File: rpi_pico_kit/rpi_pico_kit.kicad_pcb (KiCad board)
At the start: 2 copper layers, 99.1 x 99.1 mm, 195 parts, among them J1 DC Jack 5.5x2.1mm, J10 OLED Display SSD1306, J11 Conn_01x04_Male, J12 Conn_01x04_Male, J13 AudioJack-CUI-SJ-3523-SMT, J14 AudioJack-CUI-SJ-3523-SMT, J2 USB_B, J3 Conn_01x03_Male, J4 DB15_Female, J5 HDMI_A, J6 Conn_01x08_Male, J7 Conn_01x08_Male, J8 Conn_01x08_Male, J9 Micro_SD_Card_Det, Q1 DMN63D8L-7, Q2 DMN63D8L-7, Q3 DMN63D8L-7, Q4 DMN63D8L-7, Q5 DMN63D8L-7, Q6 DMN63D8L-7, Q7 DMN63D8L-7, SW1 SW_Push, SW10 SW_Push, SW2 RotaryEncoder_Switch, SW3 SW_Push, SW4 SW_Push, SW5 SW_Push, SW6 SW_Push, SW7 SW_Push, SW8 SW_Push, SW9 SW_Push, U1 RPi Pico, U10 74LVC2G34GV, U11 PCM5101A, U2 NCP1117-3.3_SOT223, U3 RP2040, U4 W25Q16JVSSIQ, U5 74HC14, U6 74HC14, U7 MCP23S08-xSO, U8 AT24CS32, U9 NCP115-3.3_SOT23-5, Y1 12MHz

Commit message: changed RPi Pico footprint in pcb
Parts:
- U1: footprint RPi_Pico:RPi_Pico_THT -> RPi_Pico:RPi_Pico_THT_socket

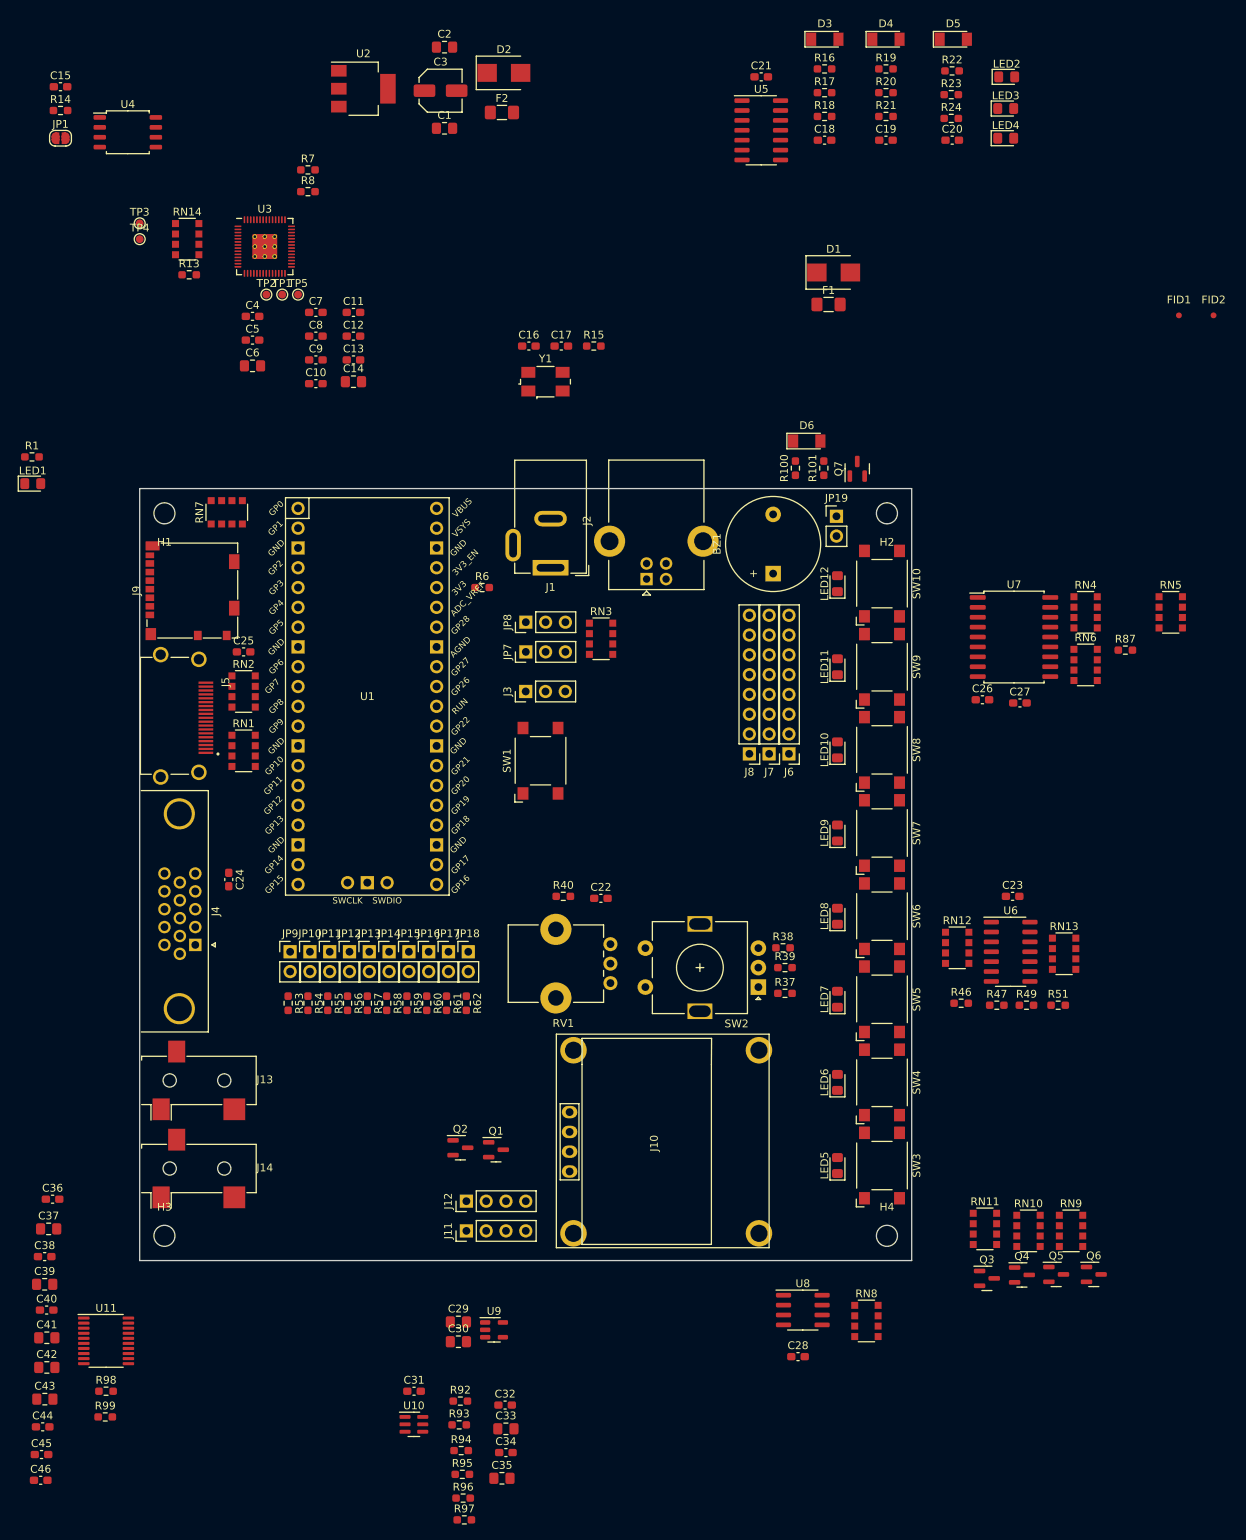
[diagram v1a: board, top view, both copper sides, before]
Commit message: changed footprints for resistor arrays
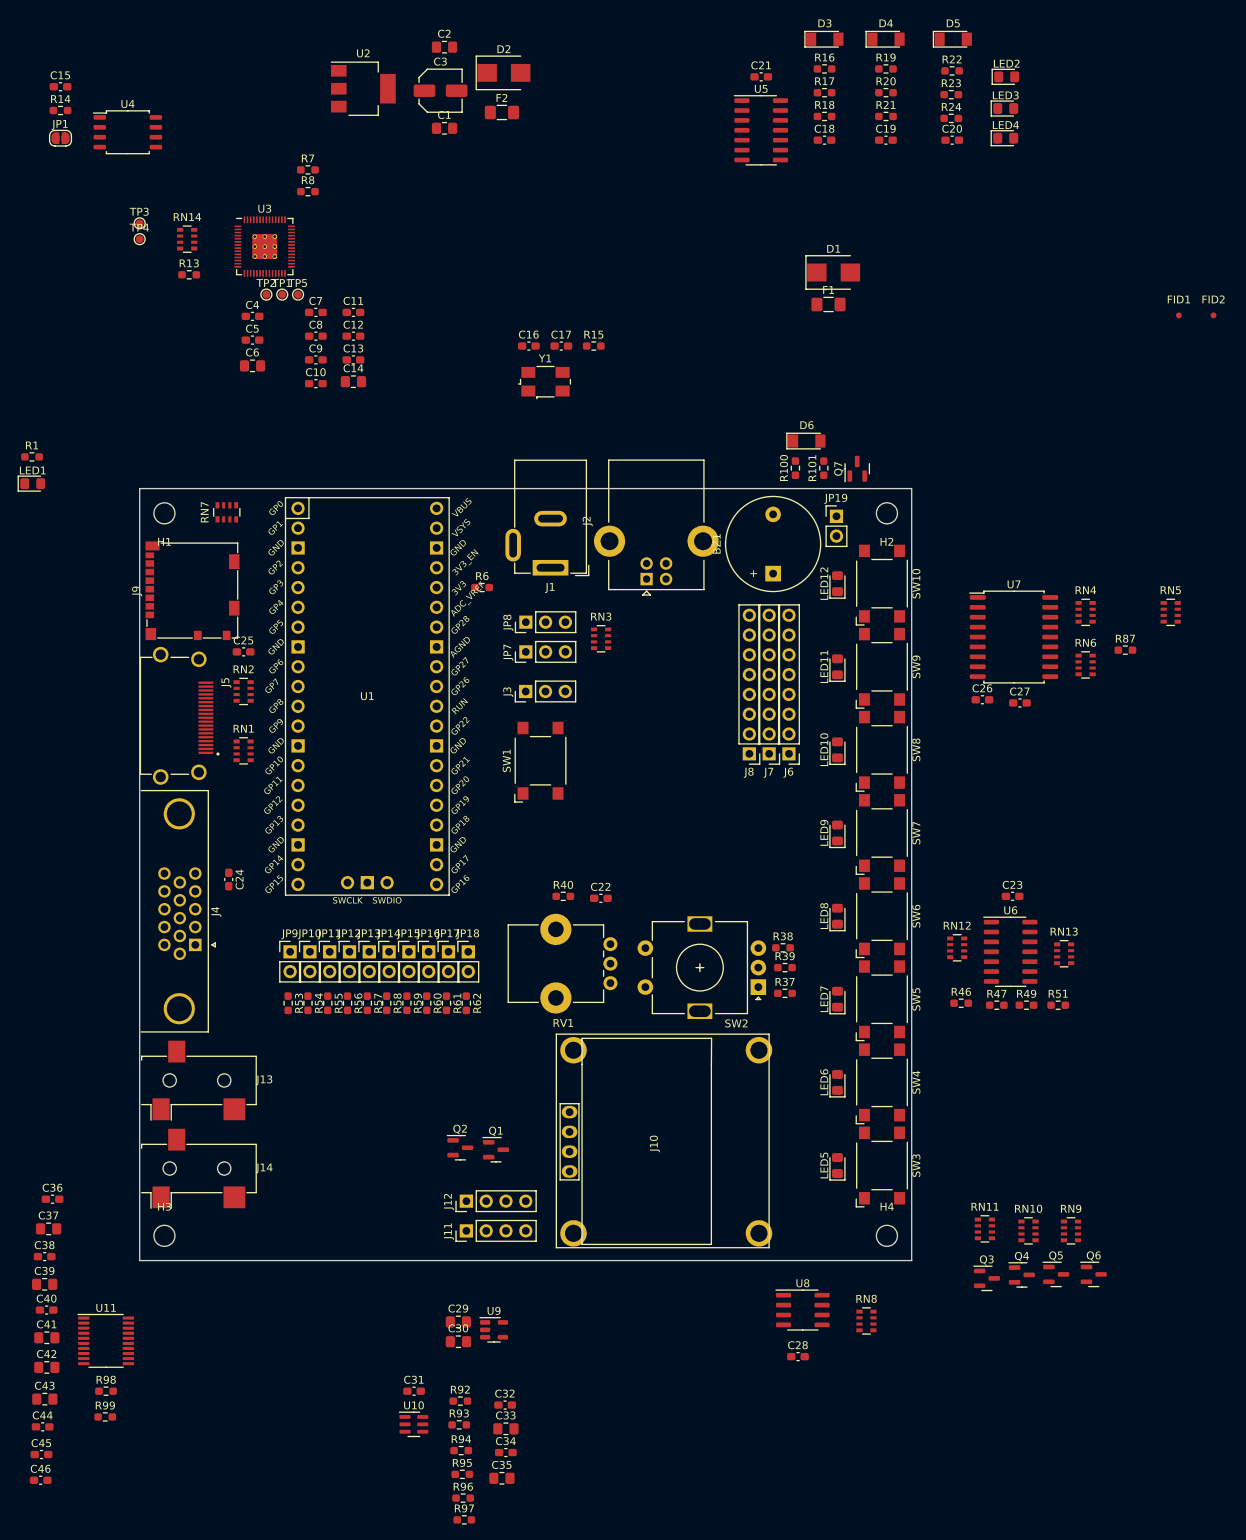
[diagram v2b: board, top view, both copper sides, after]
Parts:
- RN1, RN10, RN11, RN12, RN13, RN14, RN2, RN3, RN4, RN5, RN6, RN7, RN8, RN9: footprint Resistor_SMD:R_Array_Convex_4x1206 -> Resistor_SMD:R_Array_Convex_4x0603

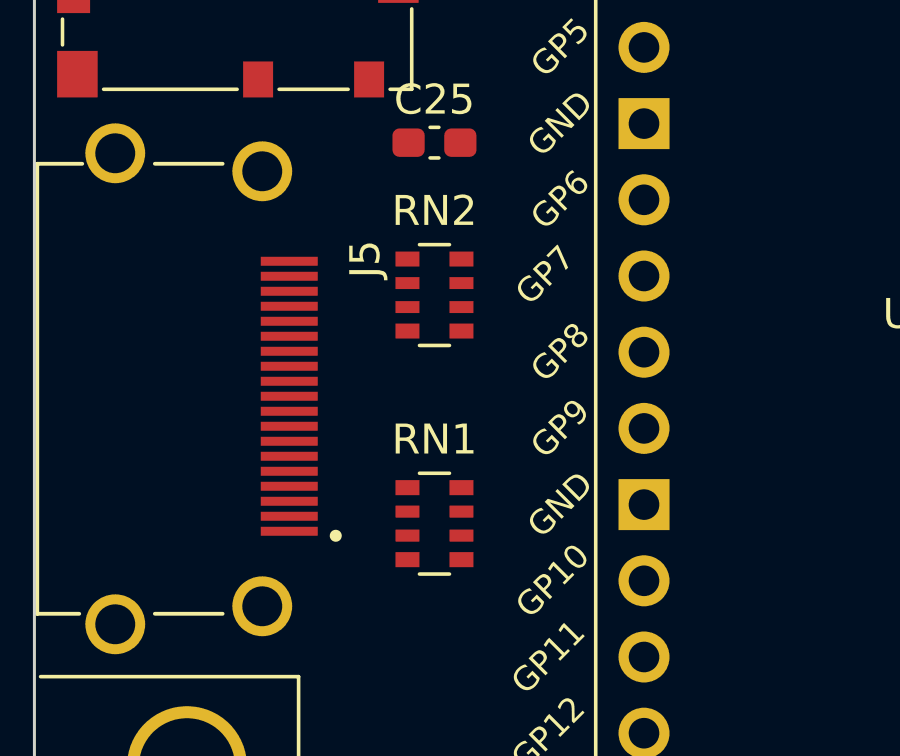
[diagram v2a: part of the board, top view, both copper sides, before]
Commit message: added names to differential pairs
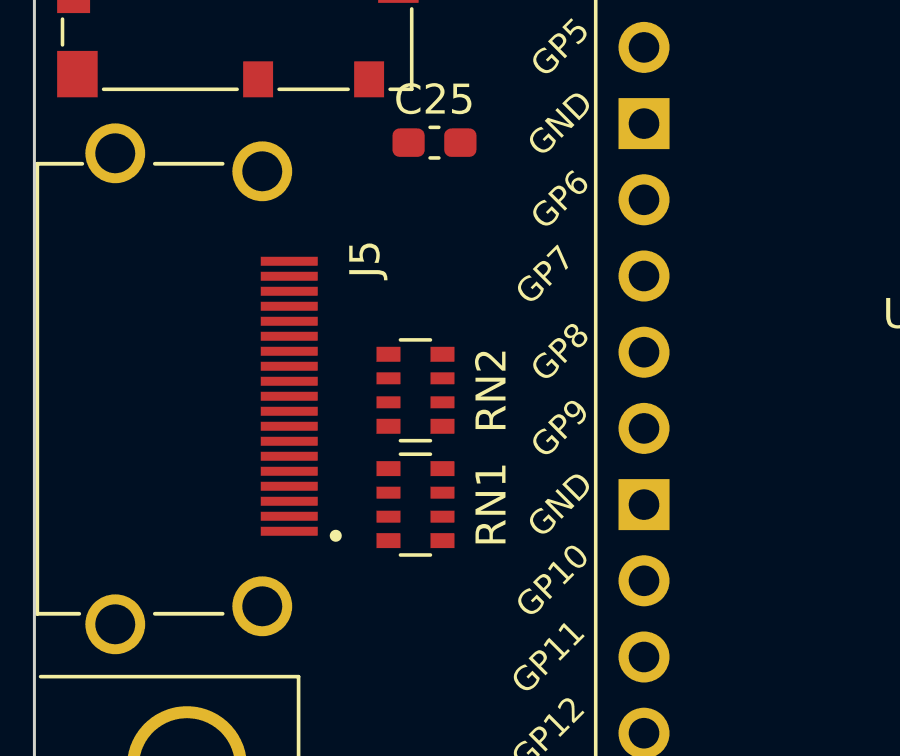
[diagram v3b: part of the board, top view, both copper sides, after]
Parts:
- moved RN2 3.24 mm to (50.8, 67.3)
- moved RN1 0.90 mm to (50.8, 71.1)
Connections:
- net Net-(J5-CK+) renamed /VGA & DVI Interface/_CLK+
- net Net-(J5-CK-) renamed /VGA & DVI Interface/_CLK-
- net Net-(J5-D0+) renamed /VGA & DVI Interface/_D0+
- net Net-(J5-D0-) renamed /VGA & DVI Interface/_D0-
- net Net-(J5-D1+) renamed /VGA & DVI Interface/_D1+
- net Net-(J5-D1-) renamed /VGA & DVI Interface/_D1-
- net Net-(J5-D2+) renamed /VGA & DVI Interface/_D2+
- net Net-(J5-D2-) renamed /VGA & DVI Interface/_D2-

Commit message: updated pcb netlist
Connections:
- net Net-(U3-USB_DM) renamed /Debugger/D-
- net Net-(U3-USB_DP) renamed /Debugger/D+

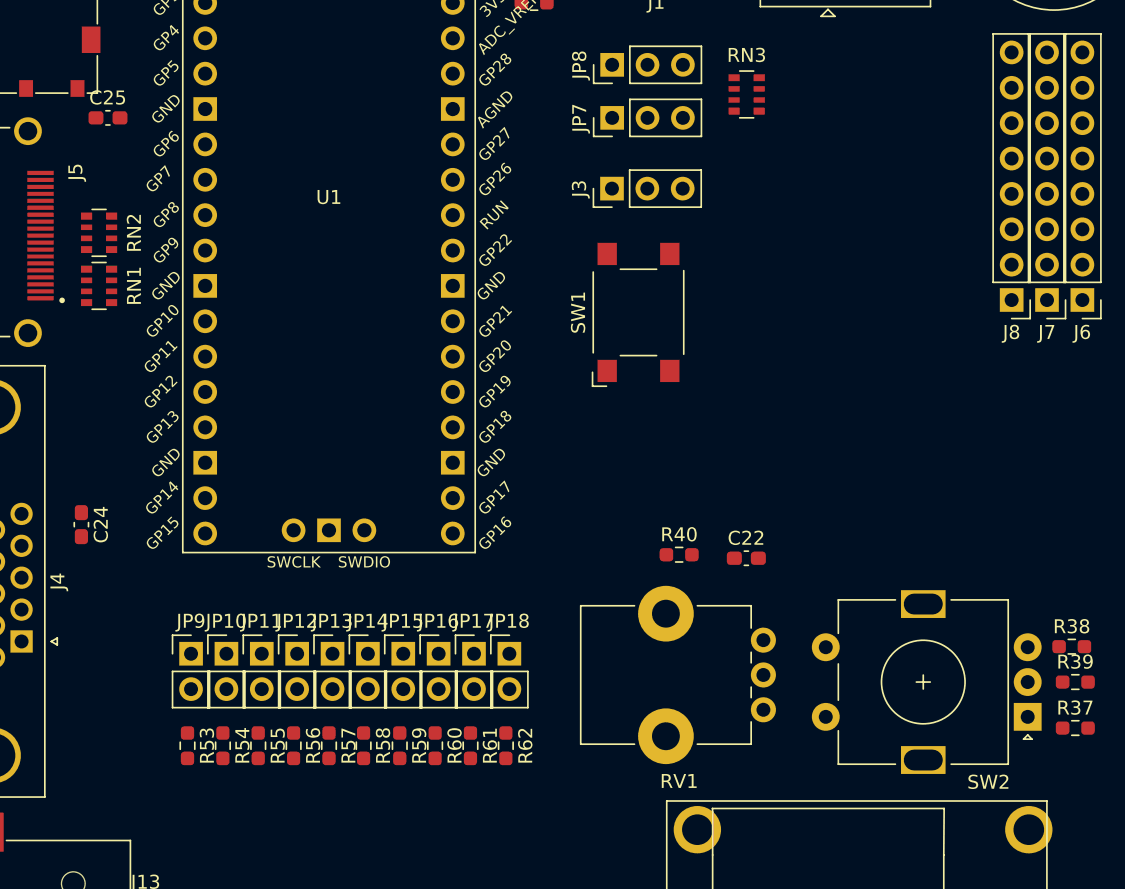
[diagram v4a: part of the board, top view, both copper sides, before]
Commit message: added net classes
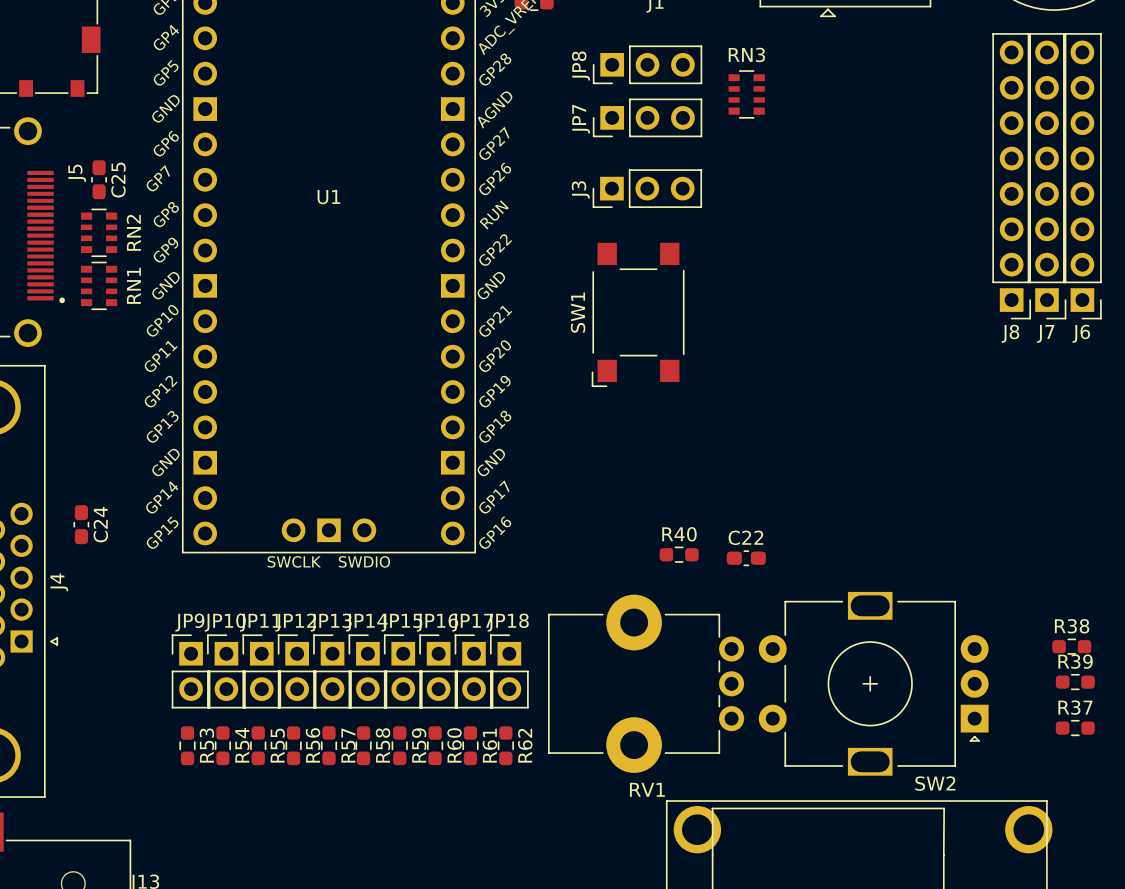
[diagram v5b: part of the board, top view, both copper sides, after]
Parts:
- moved C25 4.49 mm to (50.8, 63.5), turned to -90 degrees
- moved SW2 3.81 mm to (113.7, 102.2)
- moved RV1 2.37 mm to (96.2, 97.2)
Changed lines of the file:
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@@
 (kicad_pcb (version 20220211) (generator pcbnew)
   (general
-    (thickness 1.6)
+    (thickness 0)
   )
   (paper "A4")
@@
   )
   (setup
-    (stackup
-      (layer "F.SilkS" (type "Top Silk Screen"))
-      (layer "F.Paste" (type "Top Solder Paste"))
-      (layer "F.Mask" (type "Top Solder Mask") (thickness 0.01))
-      (layer "F.Cu" (type "copper") (thickness 0.035))
-      (layer "dielectric 1" (type "core") (thickness 1.51) (material "FR4") (epsilon_r 4.5) (loss_tangent 0.02))
-      (layer "B.Cu" (type "copper") (thickness 0.035))
-      (layer "B.Mask" (type "Bottom Solder Mask") (thickness 0.01))
-      (layer "B.Paste" (type "Bottom Solder Paste"))
-      (layer "B.SilkS" (type "Bottom Silk Screen"))
-      (copper_finish "None")
-      (dielectric_constraints no)
-    )
     (pad_to_mask_clearance 0.05)
     (pcbplotparams
@@
   )
   (footprint "Rotary_Encoder:RotaryEncoder_Alps_EC11E-Switch_Vertical_H20mm" (layer "F.Cu")
-    (at 117.486 102.068 180)
+    (at 113.676 102.195 180)
     (descr "Alps rotary encoder, EC12E... with switch, vertical shaft, http://www.alps.com/prod/info/E/HTML/Encoder/Incremental/EC11/EC11E15204A3.html")
     (tags "rotary encoder")
@@
   )
   (footprint "Capacitor_SMD:C_0603_1608Metric_Pad1.08x0.95mm_HandSolder" (layer "F.Cu")
-    (at 51.435 59.055)
+    (at 50.8 63.5 -90)
     (descr "Capacitor SMD 0603 (1608 Metric), square (rectangular) end terminal, IPC_7351 nominal with elongated pad for handsoldering. (Body size source: IPC-SM-782 page 76, https://www.pcb-3d.com/wordpress/wp-content/uploads/ipc-sm-782a_amendment_1_and_2.pdf), generated with kicad-footprint-generator")
     (tags "capacitor handsolder")
@@
     (property "Supplier Part URL" "")
     (attr smd)
-    (fp_text reference "C25" (at 0 -1.43) (layer "F.SilkS")
+    (fp_text reference "C25" (at 0 -1.43 90) (layer "F.SilkS")
         (effects (font (size 1 1) (thickness 0.15)))
     )
-    (fp_text value "100n" (at 0 1.43) (layer "F.Fab")
+    (fp_text value "100n" (at 0 1.43 90) (layer "F.Fab")
         (effects (font (size 1 1) (thickness 0.15)))
     )
-    (fp_text user "${REFERENCE}" (at 0 0) (layer "F.Fab")
+    (fp_text user "${REFERENCE}" (at 0 0 90) (layer "F.Fab")
         (effects (font (size 0.4 0.4) (thickness 0.06)))
     )
@@
     (fp_line (start 0.8 0.4) (end -0.8 0.4)
       (stroke (width 0.1) (type solid)) (layer "F.Fab"))
-    (pad "1" smd roundrect (at -0.8625 0) (size 1.075 0.95) (layers "F.Cu" "F.Paste" "F.Mask") (roundrect_rratio 0.25)
+    (pad "1" smd roundrect (at -0.8625 0 270) (size 1.075 0.95) (layers "F.Cu" "F.Paste" "F.Mask") (roundrect_rratio 0.25)
       (net 4 "+5V") (pintype "passive"))
-    (pad "2" smd roundrect (at 0.8625 0) (size 1.075 0.95) (layers "F.Cu" "F.Paste" "F.Mask") (roundrect_rratio 0.25)
+    (pad "2" smd roundrect (at 0.8625 0 270) (size 1.075 0.95) (layers "F.Cu" "F.Paste" "F.Mask") (roundrect_rratio 0.25)
       (net 3 "GND") (pintype "passive"))
     (model "${KICAD6_3DMODEL_DIR}/Capacitor_SMD.3dshapes/C_0603_1608Metric.wrl"
@@
   )
   (footprint "Potentiometer_THT:Potentiometer_Bourns_PTV09A-1_Single_Vertical" (layer "F.Cu")
-    (at 98.506 96.56 180)
+    (at 96.22 97.195 180)
     (descr "Potentiometer, vertical, Bourns PTV09A-1 Single, http://www.bourns.com/docs/Product-Datasheets/ptv09.pdf")
     (tags "Potentiometer vertical Bourns PTV09A-1 Single")
